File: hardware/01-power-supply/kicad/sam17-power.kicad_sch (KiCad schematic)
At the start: 20 parts, among them J1 12VAC CT 2A, J2 BUS +12/G/G/-12, U1 LM7812, U2 LM7912

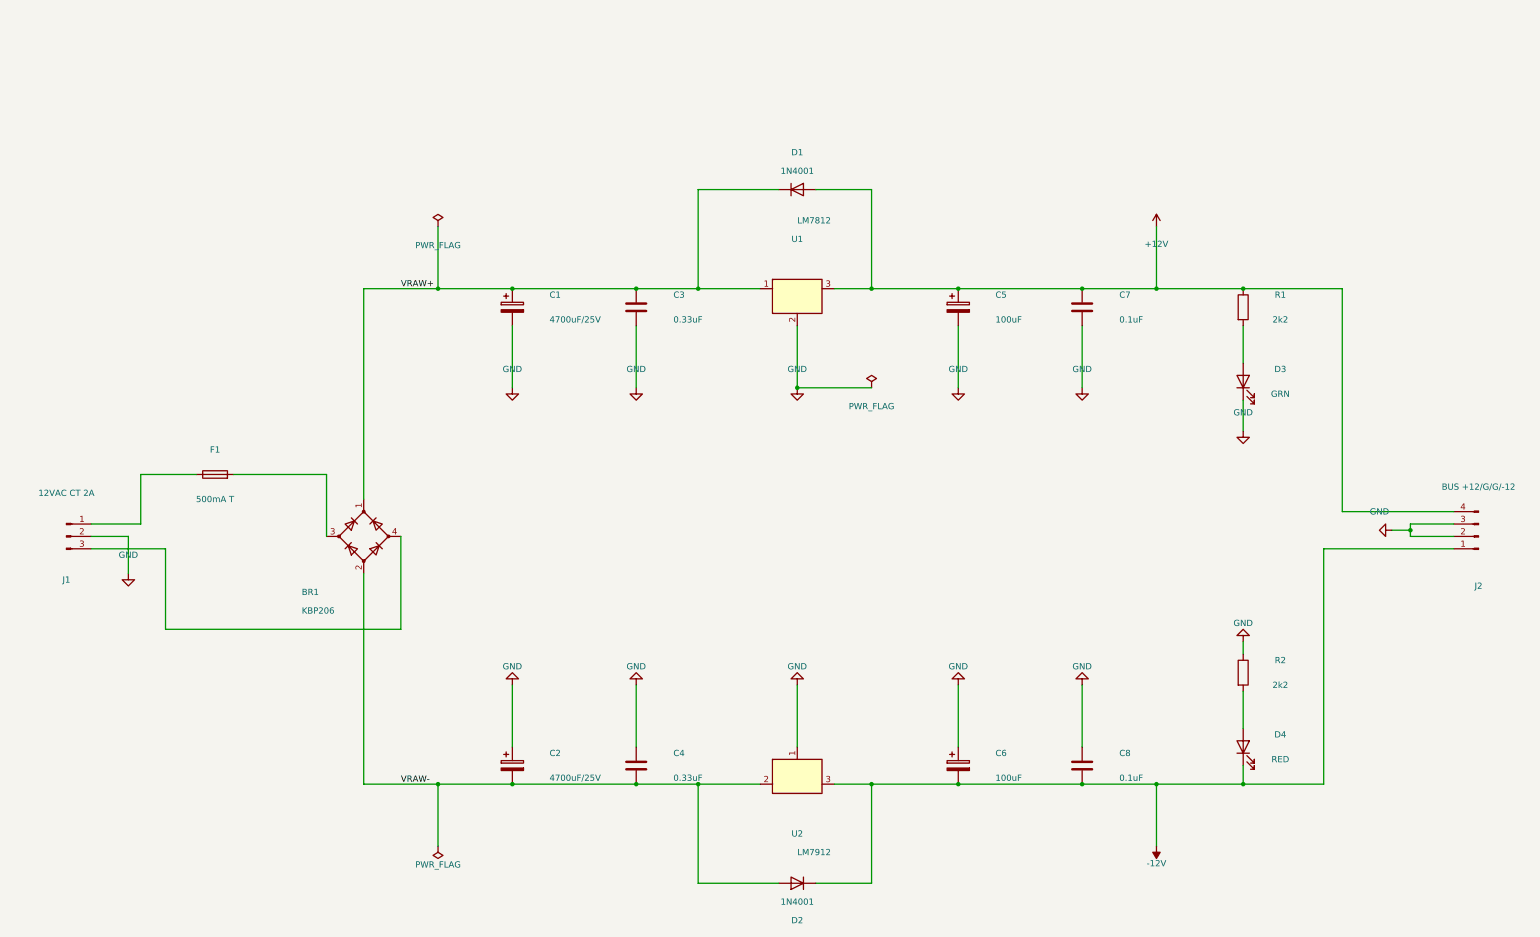
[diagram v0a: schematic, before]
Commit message: Add +5V rail, primary-side protection, and EU 230V variant to module 1
Three additions to the power supply schematic, bundled together:

- +5V rail (LM7805) for the MIDI/CV module's DAC and LCD, matching
  design-notes.md §10.1.
- Primary-side fuse/MOV/NTC soft-start protection (§10.2/§10.3), moved
  F1 to where it actually belongs (primary, not secondary — protects
  against a fault reflected from the secondary, per the design note).
- Adapted the primary stage for European mains (230VAC/50Hz) instead
  of the thesis's original Venezuelan 110VAC/60Hz: MOV swapped from
  V150LA20A (150V, fails on 230V mains) to S20K275 (275V, verified
  against the actual voltage-vs-part-number relationship), fuse
  derated 500mA->250mA for the halved primary current. The NTC needed
  no change — confirmed via the Vishay/Ametherm SL10 datasheet that
  the whole family is rated 265VAC, comfortably covering 230V+10%.
  design-notes.md §12 documents the change; §10's original Venezuela
  reasoning is left intact as historical record, not overwritten.

ERC clean (0 errors), netlist verified, LED indicator colors corrected
to match bom.csv (had invented different colors without checking it).

Known gaps, documented in the module README, not resolved here because
they need a real decision rather than a guess: J3 (mains input) has no
protective-earth pin despite bom.csv specifying one, and J1 (transformer
secondary) is 3-pin while bom.csv says 2-pin — one of the two is stale
and it's unclear which.
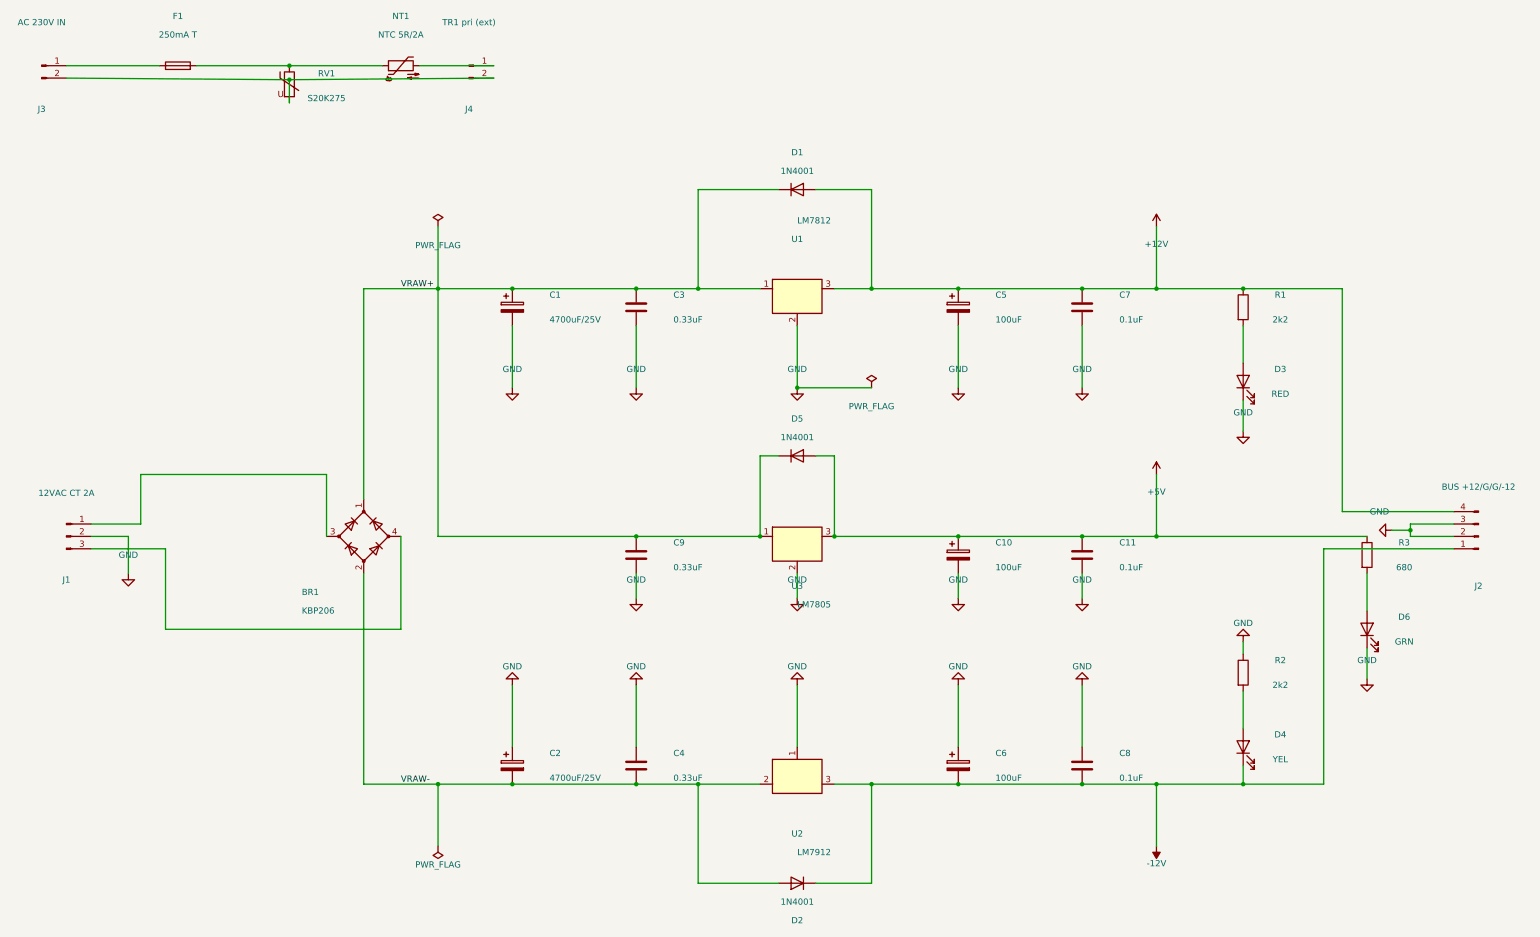
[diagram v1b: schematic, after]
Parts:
- added C10: 100uF, symbol Device:C_Polarized
- added C11: 0.1uF, symbol Device:C
- added C9: 0.33uF, symbol Device:C
- added D5: 1N4001, symbol Diode:1N4001
- added D6: GRN, symbol Device:LED
- added J3: AC 230V IN, symbol Connector:Conn_01x02_Pin
- added J4: TR1 pri (ext), symbol Connector:Conn_01x02_Pin
- added NT1: NTC 5R/2A, symbol Device:Thermistor_NTC
- added R3: 680, symbol Device:R
- added RV1: S20K275, symbol Device:Varistor
- added U3: LM7805, symbol Regulator_Linear:LM7805_TO220
- D3: value GRN -> RED
- D4: value RED -> YEL
- F1: value 500mA T -> 250mA T
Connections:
- net GND: now also C10.2, C11.2, C9.2, D6.1 (K), U3.2 (GND)
- net VRAW+: now also C9.1, D5.1 (K), U3.1 (VI)
- net at J1.1 (Pin_1): now also BR1.3; no longer F1.1
- net at F1.2: now also NT1.1, RV1.1; no longer BR1.3
- new net: F1.1, J3.1 (Pin_1)
- new net: J3.2 (Pin_2), J4.2 (Pin_2), RV1.2
- new net: J4.1 (Pin_1), NT1.2
- new net: D6.2 (A), R3.2
- new net +5V: C10.1, C11.1, D5.2 (A), R3.1, U3.3 (VO)
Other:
- title: Modulo 01 — Alimentacion ±12 V -> Modulo 01 — Alimentacion ±12 V / +5V
